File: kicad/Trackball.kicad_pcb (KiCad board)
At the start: 2 copper layers, 60 x 55 mm, 42 parts, among them J1 Conn_01x04, J101 Conn_02x03_Counter_Clockwise, J2 Conn_02x04_Counter_Clockwise, SW1 Push_Button, SW101 Push_Button, SW102 Push_Button, SW103 Push_Button, SW104 Push_Button, SW106 Push_Button, SW2 Push_Button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

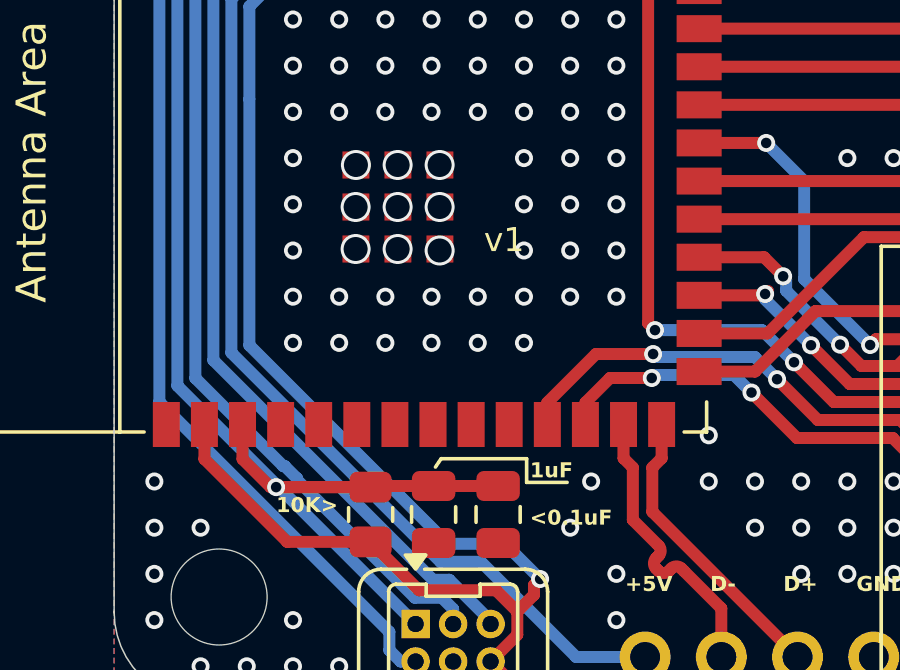
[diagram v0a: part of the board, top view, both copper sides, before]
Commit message: ajout test pad
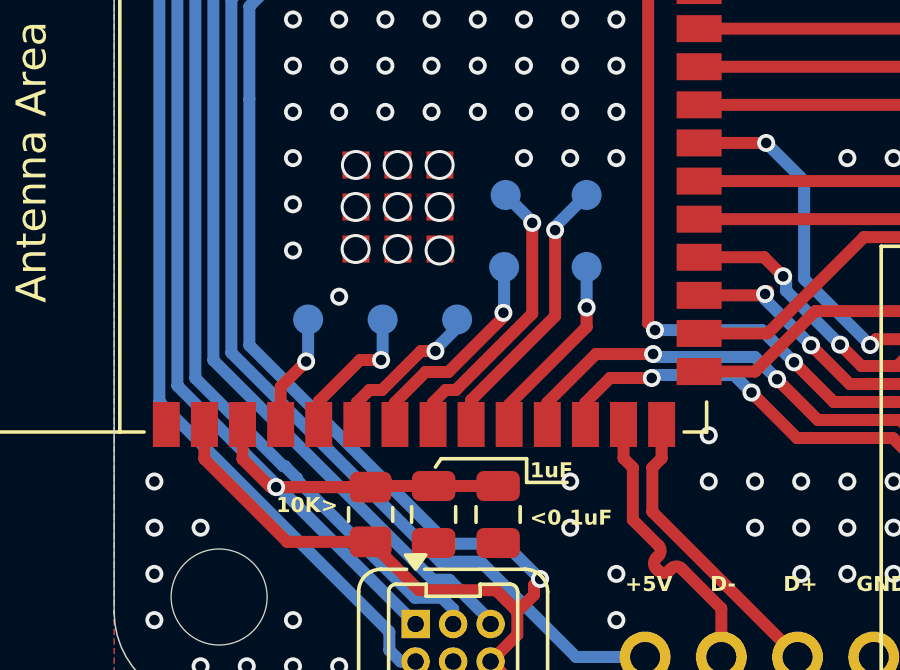
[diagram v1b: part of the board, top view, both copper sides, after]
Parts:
- added TP101: TestPoint, TestPoint:TestPoint_Pad_D1.0mm, B.Cu at (98.5, 62.8)
- added TP102: TestPoint, TestPoint:TestPoint_Pad_D1.0mm, B.Cu at (101.0, 62.8)
- added TP103: TestPoint, TestPoint:TestPoint_Pad_D1.0mm, B.Cu at (103.4, 62.8)
- added TP104: TestPoint, TestPoint:TestPoint_Pad_D1.0mm, B.Cu at (105.0, 61.0)
- added TP105: TestPoint, TestPoint:TestPoint_Pad_D1.0mm, B.Cu at (105.0, 58.6)
- added TP106: TestPoint, TestPoint:TestPoint_Pad_D1.0mm, B.Cu at (107.8, 58.6)
- added TP107: TestPoint, TestPoint:TestPoint_Pad_D1.0mm, B.Cu at (107.8, 61.0)
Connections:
- U1 pad 4: unconnected-(U1-GPIO4/TOUCH4/ADC1_CH3-Pad4) -> GPIO4
- U1 pad 5: unconnected-(U1-GPIO5/TOUCH5/ADC1_CH4-Pad5) -> GPIO5
- U1 pad 6: unconnected-(U1-GPIO6/TOUCH6/ADC1_CH5-Pad6) -> GPIO6
- U1 pad 7: unconnected-(U1-GPIO7/TOUCH7/ADC1_CH6-Pad7) -> GPIO7
- U1 pad 8: unconnected-(U1-GPIO15/U0RTS/ADC2_CH4/XTAL_32K_P-Pad8) -> GPIO15
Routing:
- net GPIO15: track 0.00 -> 9.59 mm, vias 0 -> 1
- net GPIO16: track 0.00 -> 9.24 mm, vias 0 -> 1
- net GPIO7: track 0.00 -> 7.20 mm, vias 0 -> 1
- net GPIO17: track 0.00 -> 6.32 mm, vias 0 -> 1
- net GPIO6: track 0.00 -> 5.41 mm, vias 0 -> 1
- net GPIO5: track 0.00 -> 4.79 mm, vias 0 -> 1
- net GPIO4: track 0.00 -> 3.88 mm, vias 0 -> 1
- net GND: vias 487 -> 468
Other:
- board text added: "<GPIO04"
- board text added: "<GPIO05"
- board text added: "<GPIO06"
- board text added: "<GPIO07"
- board text added: "<GPIO15"
- board text added: "<GPIO16"
- board text added: "<GPIO17"
- board text removed: "v1"

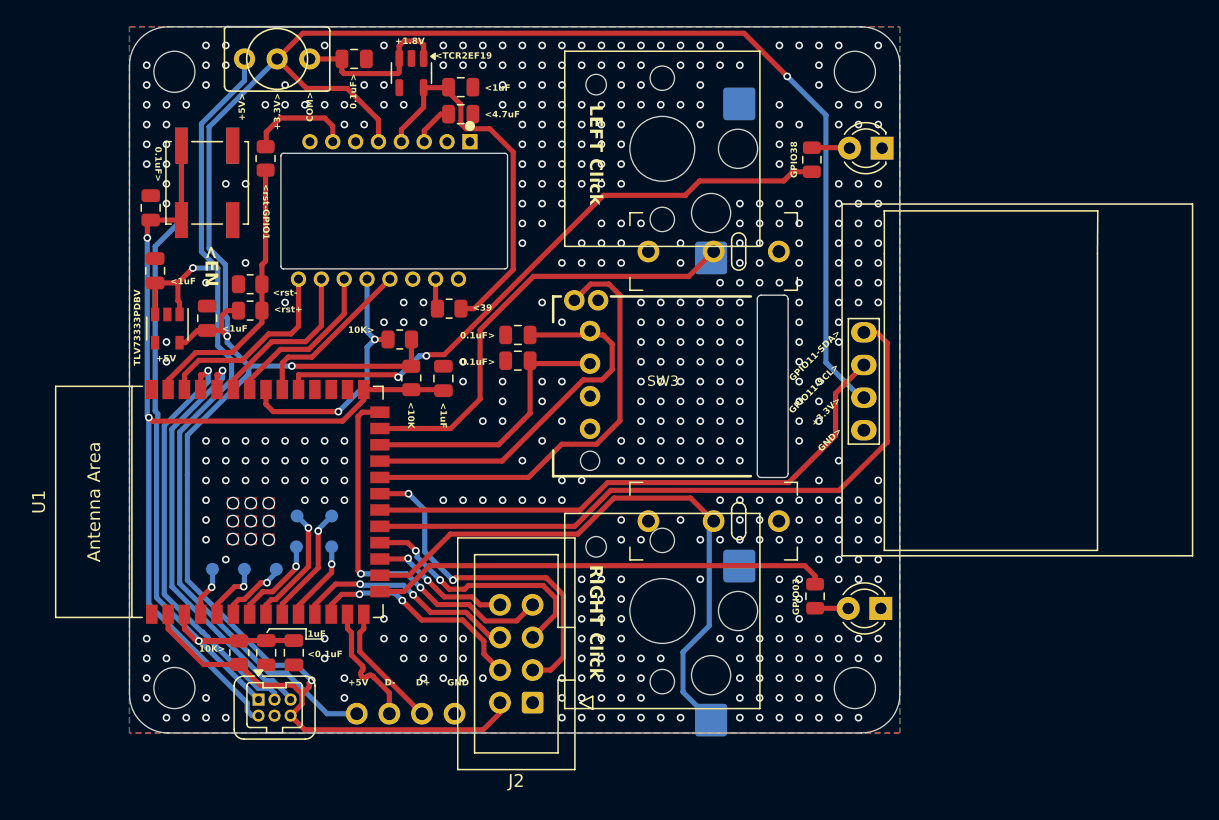
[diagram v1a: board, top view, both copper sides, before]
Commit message: re-asignement des pins gpio
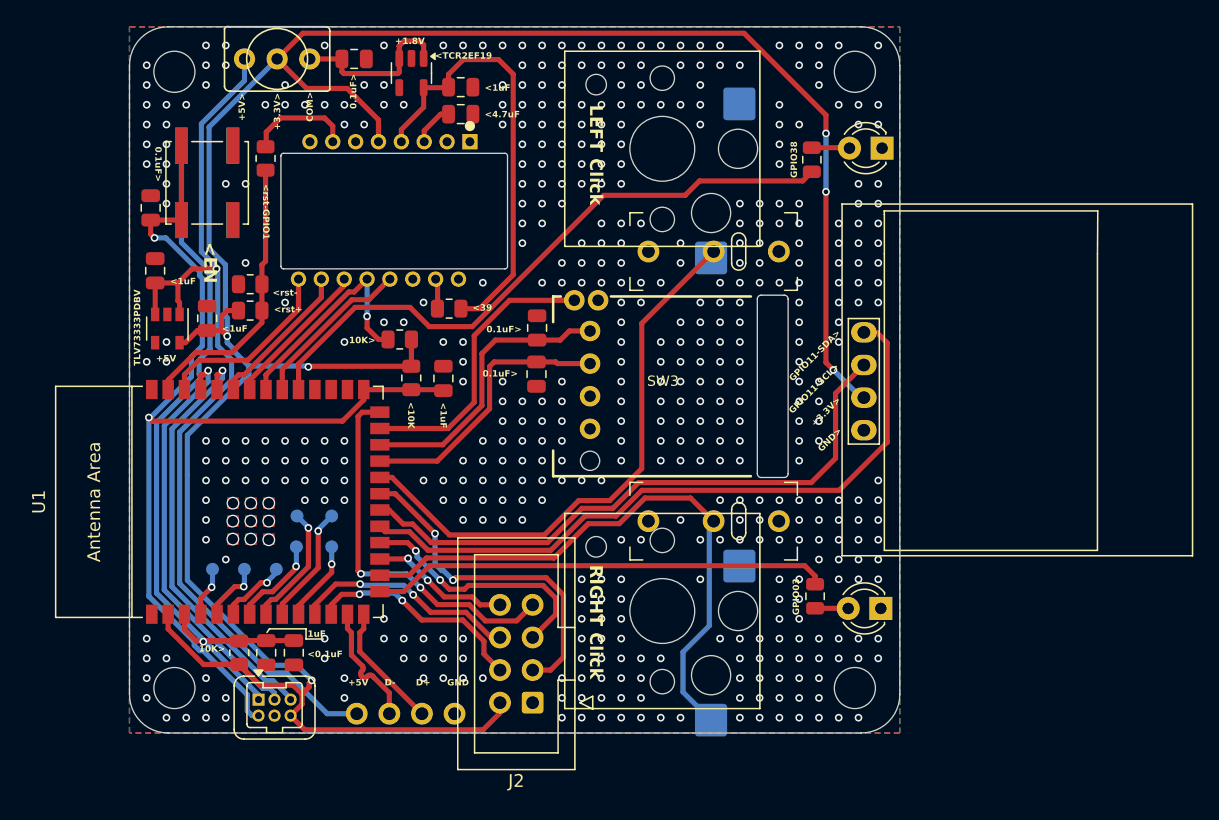
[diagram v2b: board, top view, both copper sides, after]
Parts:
- moved C102 1.79 mm to (123.7, 47.5), turned to 90 degrees
- moved C101 1.60 mm to (123.8, 44.0), turned to 90 degrees
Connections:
- C101 pad 1: GPIO21 -> GPIO37
- C102 pad 2: GPIO37 -> GPIO21
- SW1 pad 2: GPIO25 -> GPIO14
- SW101 pad 2: GPIO25 -> GPIO14
- SW3 pad A: GPIO21 -> GPIO37
- SW3 pad B: GPIO37 -> GPIO21
- SW3 pad S1: GPIO14 -> GPIO25
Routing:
- net GPIO25: track 35.5 -> 22.3 mm
- net GPIO14: track 34.7 -> 44.2 mm
- net GPIO21: track 30.2 -> 21.6 mm
- net +1V8: track 29.8 -> 34.7 mm
- net GPIO0: track 75.4 -> 79.4 mm
- net GPIO12: track 44.3 -> 47.4 mm
- net MISO: track 19.8 -> 17.9 mm, vias 2 -> 1
- net GPIO38: track 47.8 -> 49.4 mm, vias 2 -> 0
- net GPIO11: track 52.1 -> 53.7 mm
- net EN: track 60.7 -> 62.1 mm
- net MOSI: track 12.9 -> 11.7 mm
- net SCLK: track 13.0 -> 11.7 mm
- net GPIO37: track 21.6 -> 22.4 mm
- net MOTION: track 15.3 -> 14.5 mm
- net GPIO13: track 27.4 -> 26.8 mm
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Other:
- board text added: "<GPIO14"
- board text added: "Push_GPIO25>"
- board text removed: "<GPIO25"
- board text removed: "Push_GPIO21>"
